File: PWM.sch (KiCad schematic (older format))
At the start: 9 parts, among them U1 74AHC132, U3 74FCT163, U4 74FCT163, U5 74FCT163, U6 74F85, U7 74F85, U8 74F85, U9 74HC74

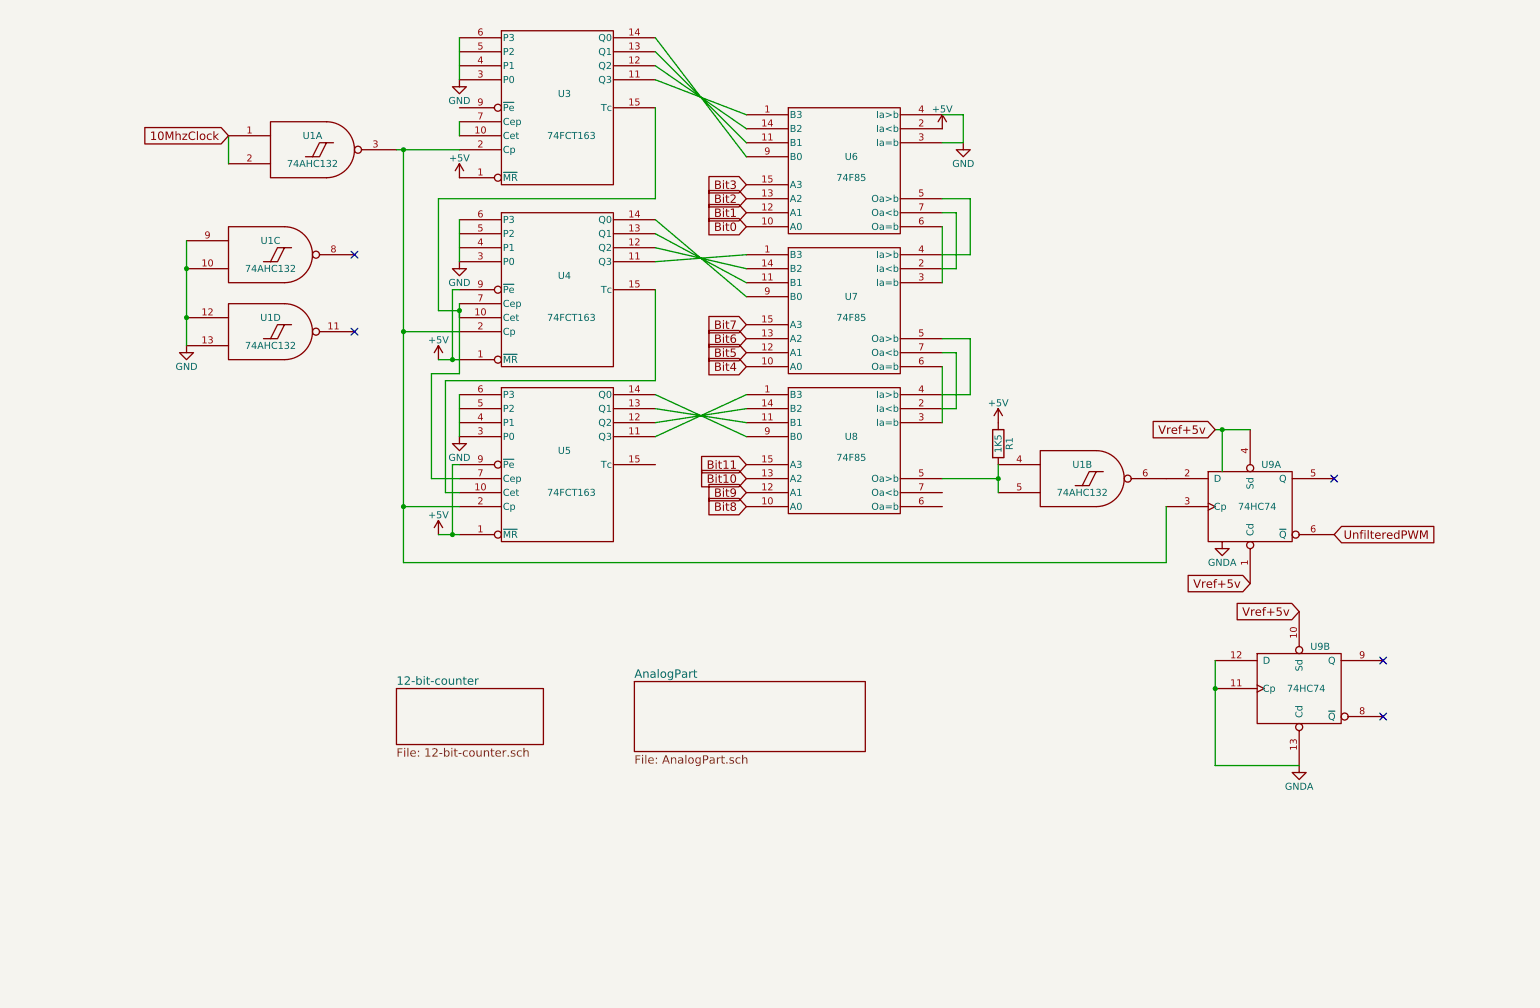
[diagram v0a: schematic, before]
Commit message: Version 1. Directly drive PWM filter using 74hc74 flip flop
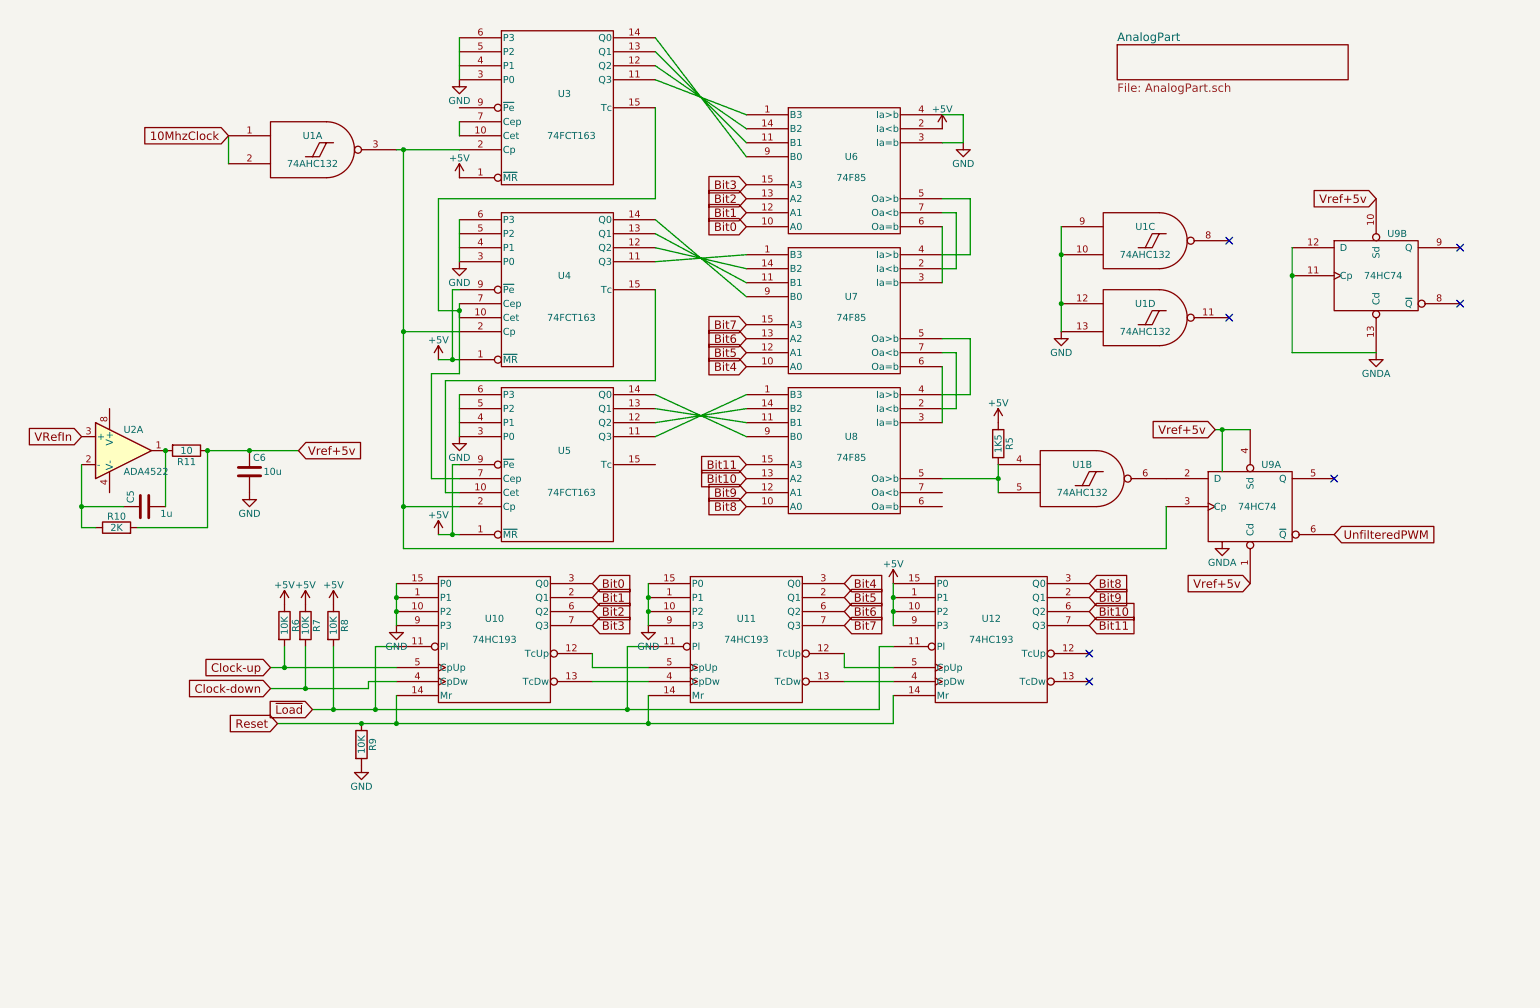
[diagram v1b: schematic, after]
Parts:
- added C5: 1u, symbol C
- added C6: 10u, symbol C
- added R10: 2K, symbol R
- added R11: 10, symbol R
- added R6, R7, R8, R9: 10K, symbol R
- added U10, U11, U12: 74HC193, symbol 74LS193
- added U2: ADA4522, symbol ADA4075
- renumbered R1 to R5
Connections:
- net +5V: now also R6.1, R7.1, R8.1, U12.1 (P1), U12.10 (P2), U12.15 (P0), U12.9 (P3)
- net Bit0: now also U10.3 (Q0)
- net Bit1: now also U10.2 (Q1)
- net Bit10: now also U12.6 (Q2)
- net Bit11: now also U12.7 (Q3)
- net Bit2: now also U10.6 (Q2)
- net Bit3: now also U10.7 (Q3)
- net Bit4: now also U11.3 (Q0)
- net Bit5: now also U11.2 (Q1)
- net Bit6: now also U11.6 (Q2)
- net Bit7: now also U11.7 (Q3)
- net Bit8: now also U12.3 (Q0)
- net Bit9: now also U12.2 (Q1)
- net GND: now also C6.2, R9.2, U10.1 (P1), U10.10 (P2), U10.15 (P0), U10.8 (GND), U10.9 (P3), U11.1 (P1), U11.10 (P2), U11.15 (P0), U11.8 (GND), U11.9 (P3), U12.8 (GND)
- net VCC: now also C6.1, R10.2, R11.1, U10.16 (VCC), U11.16 (VCC), U12.16 (VCC)
- new net: C5.2, R11.2, U2.1
- new net: C5.1, R10.1, U2.2 (-)
- new net: U10.12 (TcUp), U11.5 (CpUp)
- new net: U10.13 (TcDw), U11.4 (CpDw)
- new net: U11.12 (TcUp), U12.5 (CpUp)
- new net: U11.13 (TcDw), U12.4 (CpDw)
- new net Clock-down: R7.2, U10.4 (CpDw)
- new net Clock-up: R6.2, U10.5 (CpUp)
- new net Reset: R9.1, U10.14 (Mr), U11.14 (Mr), U12.14 (Mr)
- new net VRefIn: U2.3 (+)
- new net ~Load: R8.2, U10.11 (Pl), U11.11 (Pl), U12.11 (Pl)
- no-connect marks 5 -> 7
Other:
- moved on the sheet: U1C, U1D, U9B

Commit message: Version 2. Use cmos logic only. Show time budget.
Eschew F85.
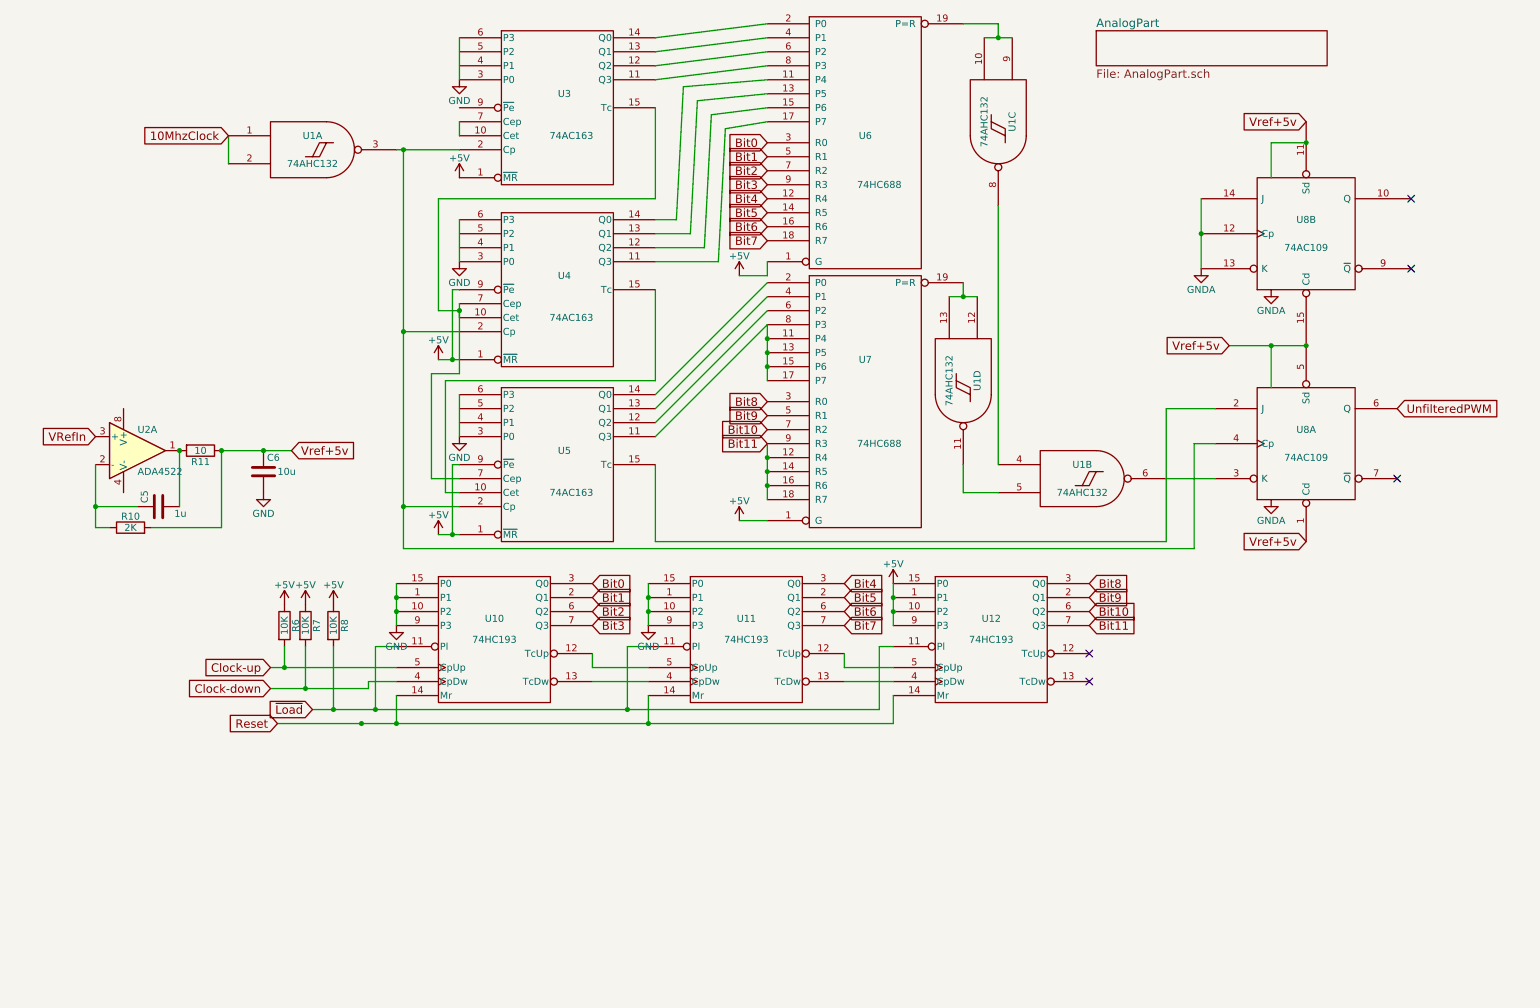
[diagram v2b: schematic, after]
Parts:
- removed R5: 1K5, symbol R
- removed R9: 10K, symbol R
- removed U6, U7, U8: 74F85, symbol 74LS85
- removed U9: 74HC74, symbol 74LS74
- added U6, U7: 74HC688, symbol 74LS688
- added U8: 74AC109, symbol 74LS109
- U3, U4, U5: value 74FCT163 -> 74AC163
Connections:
- net +5V: now also U6.1 (G), U7.1 (G)
- net Bit0: now also U6.3 (R0)
- net Bit1: now also U6.5 (R1)
- net Bit10: now also U7.7 (R2)
- net Bit11: now also U7.12 (R4), U7.14 (R5), U7.16 (R6), U7.18 (R7), U7.9 (R3)
- net Bit2: now also U6.7 (R2)
- net Bit3: now also U6.9 (R3)
- net Bit4: now also U6.12 (R4)
- net Bit5: now also U6.14 (R5)
- net Bit6: now also U6.16 (R6)
- net Bit7: now also U6.18 (R7)
- net Bit8: now also U7.3 (R0)
- net Bit9: now also U7.5 (R1)
- net GND: now also U6.10 (GND), U7.10 (GND), U8.12 (Cp), U8.13 (K), U8.14 (J), U8.8 (GND), U8.8 (GND); no longer U1.10, U1.12, U1.13, U1.9
- net UnfilteredPWM: now also U8.6 (Q)
- net VCC: now also U6.20 (VCC), U7.20 (VCC), U8.1 (Cd), U8.11 (Sd), U8.15 (Cd), U8.16 (VCC), U8.16 (VCC), U8.5 (Sd)
- net at U3.11 (Q3): now also U6.8 (P3)
- net at U3.12 (Q2): now also U6.6 (P2)
- net at U3.13 (Q1): now also U6.4 (P1)
- net at U3.14 (Q0): now also U6.2 (P0)
- net at U1.3, U3.2 (Cp), U4.2 (Cp)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: now also U8.4 (Cp)
- net at U1.6: now also U8.3 (K)
- net at U4.11 (Q3): now also U6.17 (P7)
- net at U4.12 (Q2): now also U6.15 (P6)
- net at U4.13 (Q1): now also U6.13 (P5)
- net at U4.14 (Q0): now also U6.11 (P4)
- net at U5.11 (Q3): now also U7.11 (P4), U7.13 (P5), U7.15 (P6), U7.17 (P7), U7.8 (P3)
- net at U5.12 (Q2): now also U7.6 (P2)
- net at U5.13 (Q1): now also U7.4 (P1)
- net at U5.14 (Q0): now also U7.2 (P0)
- net at U5.15 (Tc): now also U8.2 (J)
- net at U1.4: now also U1.8; no longer U1.5
- net at U1.11: now also U1.5
- new net: U1.10, U1.9, U6.19 (P=R)
- new net: U1.12, U1.13, U7.19 (P=R)
- no-connect marks 7 -> 5
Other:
- moved on the sheet: C5, C6, R10, R11, U1C, U1D, U2A

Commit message: Added version 3 files
Tested, working as of 3.25.2018. Tested using IXDD609 gate driver.
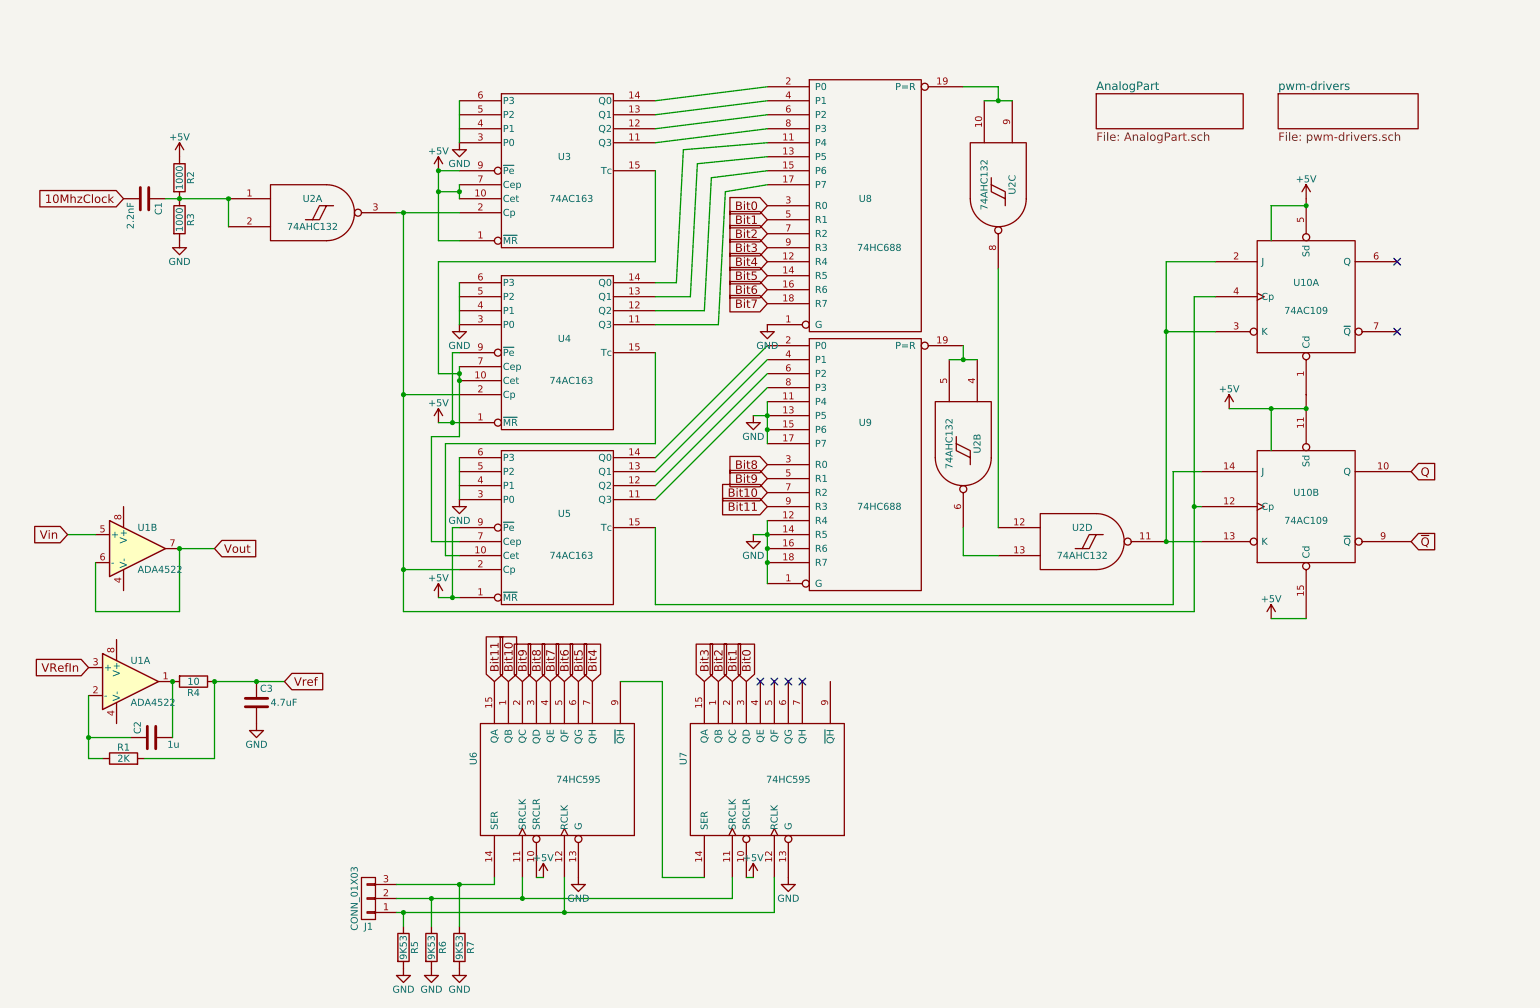
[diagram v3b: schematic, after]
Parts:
- removed R8: 10K, symbol R
- removed U10, U11, U12: 74HC193, symbol 74LS193
- added C1: 2.2nF, symbol C
- added J1: CONN_01X03, symbol CONN_01X03
- added R2, R3: 1000, symbol R
- added R5: 9K53, symbol R
- added unit 2 of U1
- added U6, U7: 74HC595, symbol 74HC595
- C3: renamed from C6; value 10u -> 4.7uF
- R6, R7: value 10K -> 9K53
- renumbered C5 to C2, R10 to R1, R11 to R4, U2 to U1, U8 to U10, U1 to U2, U6 to U8, U7 to U9
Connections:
- net Clock-down is gone; now on net GND: R7.2
- net Clock-up is gone; now on net GND: R6.2
- net +5V: now also U10.15 (Cd), U10.16 (VCC), U10.16 (VCC), U10.5 (Sd), U2.14 (VCC), U2.14 (VCC), U2.14 (VCC), U2.14 (VCC), U3.10 (Cet), U3.16 (VCC), U3.7 (Cep), U3.9 (~Pe), U4.16 (VCC), U5.16 (VCC), U8.20 (VCC), U9.20 (VCC), R2.1, U6.10 (SRCLR), U6.16 (VCC), U7.10 (SRCLR), U7.16 (VCC); no longer R6.1, R7.1, U8.1 (G), U9.1 (G)
- net 10MhzClock: now also C1.2; no longer U2.1, U2.2
- net Bit0: now also U7.3 (QD)
- net Bit1: now also U7.2 (QC)
- net Bit10: now also U6.1 (QB)
- net Bit11: now also U6.15 (QA); no longer U9.12 (R4), U9.14 (R5), U9.16 (R6), U9.18 (R7)
- net Bit2: now also U7.1 (QB)
- net Bit3: now also U7.15 (QA)
- net Bit4: now also U6.7 (QH)
- net Bit5: now also U6.6 (QG)
- net Bit6: now also U6.5 (QF)
- net Bit7: now also U6.4 (QE)
- net Bit8: now also U6.3 (QD)
- net Bit9: now also U6.2 (QC)
- net GND: now also U8.1 (G), U9.1 (G), U9.11 (P4), U9.12 (R4), U9.13 (P5), U9.14 (R5), U9.15 (P6), U9.16 (R6), U9.17 (P7), U9.18 (R7), R3.2, R5.2, U6.13 (G), U6.8 (GND), U7.13 (G), U7.8 (GND); no longer U10.12 (Cp), U10.13 (K), U10.14 (J)
- net at U2.3, U3.2 (Cp), U4.2 (Cp)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: now also U10.12 (Cp), U10.4 (Cp); no longer U10.4 (Cp)
- net at U5.15 (Tc): now also U10.14 (J); no longer U10.2 (J)
- net at U2.4: now also U2.5, U9.19 (P=R); no longer U2.8
- net at U2.6: now also U2.13; no longer U10.3 (K)
- removed net UnfilteredPWM: U10.6 (Q)
- removed net VCC: C3.1, R1.2, R4.1, U10.1 (Cd), U10.11 (Sd), U10.15 (Cd), U10.16 (VCC), U10.16 (VCC), U10.5 (Sd), U2.14 (VCC), U2.14 (VCC), U2.14 (VCC), U2.14 (VCC), U3.16 (VCC), U4.16 (VCC), U5.16 (VCC), U8.20 (VCC), U9.20 (VCC)
- new net: U5.11 (Q3), U9.8 (P3)
- new net: C1.1, R2.2, R3.1, U2.1, U2.2
- new net: U10.13 (K), U10.2 (J), U10.3 (K), U2.11
- new net: U2.12, U2.8
- new net: U2.10, U2.9, U8.19 (P=R)
- new net: U10.1 (Cd), U10.11 (Sd)
- new net: J1.2 (P2), R6.1, U6.11 (SRCLK), U7.11 (SRCLK)
- new net: J1.1 (P1), R5.1, U6.12 (RCLK), U7.12 (RCLK)
- new net: J1.3 (P3), R7.1, U6.14 (SER)
- new net: U6.9 (~QH), U7.14 (SER)
- new net Q: U10.10 (Q)
- new net Vin: U1.5 (+)
- new net Vout: U1.6 (-), U1.7
- new net Vref: C3.1, R1.2, R4.1
- new net ~Q: U10.9 (~Q)
- no-connect marks 5 -> 6
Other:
- moved on the sheet: C2, C3, R1, R4, U1A, U2A, U2B, U3, U4, U5, U8, U9
